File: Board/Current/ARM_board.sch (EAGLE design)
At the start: 157 parts, among them IC3 STM32F437VI, IC4 LM358DT, J1 USART/I2C, J10 ANALOG, J11 DGND, J12 DPWR, J13 DIGITAL, J14 SGND, J15 SPWR, J16 SERVO, J2 I2C2/USART3, J3 USART2, J5 SPI, J6 Bluesmirf, J7 SWD, J8 AGND, J9 APWR, Q1 STL4P2UH7, Q2 2STR1230, SW1 SW, U1 LSM330DLC, U10 BAV99, U11 BAV99, U12 USBLC6-2, U13 USBLC6-2, U14 STMPS2171MTR, U15 MC74HC164, U16 STL85N6F3, U17 ZENER-BZX384C20-E3-08, U18 ZENER-BZX384C20-E3-08, U2 RT7259, U3 NC7SZU04, U4 L6206Q, U5 L6206Q, U6 SI7617, U7 SI7617, U8 SI7617, U9 SI7617, Y2 8MHz

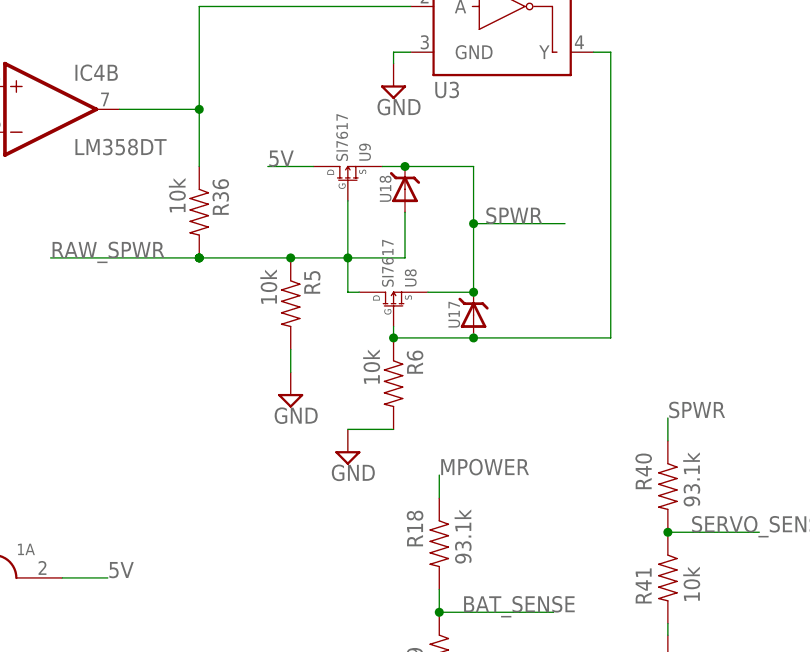
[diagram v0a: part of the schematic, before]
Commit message: Added green box 30mil inside the board outline and moved all traces within the line. Removed the extra space that was added around the board for the previous revision. Removed the zener diodes for now (need to re-evaluate them).
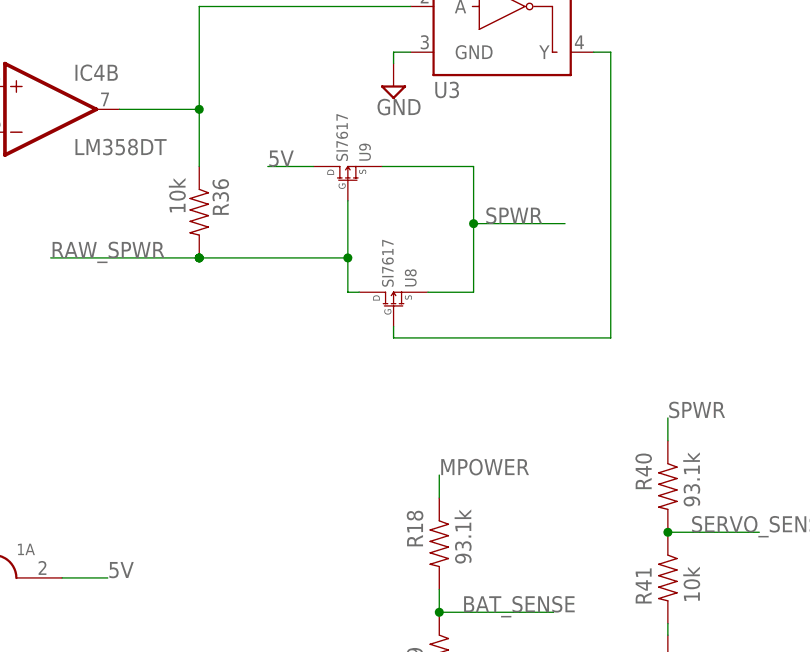
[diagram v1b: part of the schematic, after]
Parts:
- removed R5, R6: 10k, SparkFun:RESISTOR0402-RES
- removed U17, U18: ZENER-BZX384C20-E3-08, zener-BZX384C20-E3-08:ZENER-BZX384C20-E3-08
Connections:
- net GND: no longer R5.2, R6.2
- net N$30: no longer R6.1, U17.P$2
- net RAW_SPWR: no longer R5.1, U18.P$2
- net SPWR: no longer U17.P$1, U18.P$1
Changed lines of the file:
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@@
 <?xml version="1.0" encoding="utf-8"?>
 <!DOCTYPE eagle SYSTEM "eagle.dtd">
-<eagle version="6.5.0">
+<eagle version="6.3">
 <drawing>
 <settings>
@@
 <grid distance="0.1" unitdist="inch" unit="inch" style="lines" multiple="1" display="no" altdistance="0.01" altunitdist="inch" altunit="inch"/>
 <layers>
-<layer number="1" name="Top" color="4" fill="1" visible="no" active="no"/>
-<layer number="16" name="Bottom" color="1" fill="1" visible="no" active="no"/>
-<layer number="17" name="Pads" color="2" fill="1" visible="no" active="no"/>
-<layer number="18" name="Vias" color="2" fill="1" visible="no" active="no"/>
-<layer number="19" name="Unrouted" color="6" fill="1" visible="no" active="no"/>
-<layer number="20" name="Dimension" color="15" fill="1" visible="no" active="no"/>
-<layer number="21" name="tPlace" color="7" fill="1" visible="no" active="no"/>
-<layer number="22" name="bPlace" color="7" fill="1" visible="no" active="no"/>
-<layer number="23" name="tOrigins" color="15" fill="1" visible="no" active="no"/>
-<layer number="24" name="bOrigins" color="15" fill="1" visible="no" active="no"/>
-<layer number="25" name="tNames" color="7" fill="1" visible="no" active="no"/>
-<layer number="26" name="bNames" color="7" fill="1" visible="no" active="no"/>
-<layer number="27" name="tValues" color="7" fill="1" visible="no" active="no"/>
-<layer number="28" name="bValues" color="7" fill="1" visible="no" active="no"/>
+<layer number="1" name="Top" color="4" fill="1" visible="yes" active="no"/>
+<layer number="16" name="Bottom" color="1" fill="1" visible="yes" active="no"/>
+<layer number="17" name="Pads" color="2" fill="1" visible="yes" active="no"/>
+<layer number="18" name="Vias" color="2" fill="1" visible="yes" active="no"/>
+<layer number="19" name="Unrouted" color="6" fill="1" visible="yes" active="no"/>
+<layer number="20" name="Dimension" color="15" fill="1" visible="yes" active="no"/>
+<layer number="21" name="tPlace" color="15" fill="1" visible="yes" active="no"/>
+<layer number="22" name="bPlace" color="7" fill="1" visible="yes" active="no"/>
+<layer number="23" name="tOrigins" color="15" fill="1" visible="yes" active="no"/>
+<layer number="24" name="bOrigins" color="15" fill="1" visible="yes" active="no"/>
+<layer number="25" name="tNames" color="15" fill="1" visible="yes" active="no"/>
+<layer number="26" name="bNames" color="7" fill="1" visible="yes" active="no"/>
+<layer number="27" name="tValues" color="7" fill="1" visible="yes" active="no"/>
+<layer number="28" name="bValues" color="7" fill="1" visible="yes" active="no"/>
 <layer number="29" name="tStop" color="7" fill="3" visible="no" active="no"/>
 <layer number="30" name="bStop" color="7" fill="6" visible="no" active="no"/>
-<layer number="31" name="tCream" color="7" fill="4" visible="no" active="no"/>
+<layer number="31" name="tCream" color="15" fill="1" visible="no" active="no"/>
 <layer number="32" name="bCream" color="7" fill="5" visible="no" active="no"/>
 <layer number="33" name="tFinish" color="6" fill="3" visible="no" active="no"/>
@@
 <layer number="35" name="tGlue" color="7" fill="4" visible="no" active="no"/>
 <layer number="36" name="bGlue" color="7" fill="5" visible="no" active="no"/>
-<layer number="37" name="tTest" color="7" fill="1" visible="no" active="no"/>
-<layer number="38" name="bTest" color="7" fill="1" visible="no" active="no"/>
+<layer number="37" name="tTest" color="7" fill="1" visible="yes" active="no"/>
+<layer number="38" name="bTest" color="7" fill="1" visible="yes" active="no"/>
 <layer number="39" name="tKeepout" color="4" fill="11" visible="no" active="no"/>
 <layer number="40" name="bKeepout" color="1" fill="11" visible="no" active="no"/>
@@
 <layer number="44" name="Drills" color="7" fill="1" visible="no" active="no"/>
 <layer number="45" name="Holes" color="7" fill="1" visible="no" active="no"/>
-<layer number="46" name="Milling" color="3" fill="1" visible="no" active="no"/>
-<layer number="47" name="Measures" color="7" fill="1" visible="no" active="no"/>
-<layer number="48" name="Document" color="7" fill="1" visible="no" active="no"/>
-<layer number="49" name="Reference" color="7" fill="1" visible="no" active="no"/>
-<layer number="50" name="dxf" color="7" fill="1" visible="no" active="no"/>
-<layer number="51" name="tDocu" color="7" fill="1" visible="no" active="no"/>
-<layer number="52" name="bDocu" color="7" fill="1" visible="no" active="no"/>
-<layer number="53" name="tGND_GNDA" color="7" fill="9" visible="no" active="no"/>
-<layer number="54" name="bGND_GNDA" color="1" fill="9" visible="no" active="no"/>
-<layer number="56" name="wert" color="7" fill="1" visible="no" active="no"/>
+<layer number="46" name="Milling" color="3" fill="1" visible="yes" active="no"/>
+<layer number="47" name="Measures" color="7" fill="1" visible="yes" active="no"/>
+<layer number="48" name="Document" color="12" fill="1" visible="yes" active="no"/>
+<layer number="49" name="Reference" color="7" fill="1" visible="yes" active="no"/>
+<layer number="50" name="dxf" color="7" fill="1" visible="yes" active="no"/>
+<layer number="51" name="tDocu" color="7" fill="1" visible="yes" active="no"/>
+<layer number="52" name="bDocu" color="7" fill="1" visible="yes" active="no"/>
+<layer number="53" name="tGND_GNDA" color="7" fill="9" visible="yes" active="no"/>
+<layer number="54" name="bGND_GNDA" color="1" fill="9" visible="yes" active="no"/>
+<layer number="56" name="wert" color="7" fill="1" visible="yes" active="no"/>
 <layer number="91" name="Nets" color="2" fill="1" visible="yes" active="yes"/>
 <layer number="92" name="Busses" color="1" fill="1" visible="yes" active="yes"/>
@@
 <part name="R37" library="SparkFun-Resistors" deviceset="RESISTOR" device="0603-RES" value="3k"/>
 <part name="R38" library="SparkFun-Resistors" deviceset="RESISTOR" device="0603-RES" value="3k"/>
-<part name="U17" library="zener-BZX384C20-E3-08" deviceset="ZENER-BZX384C20-E3-08" device=""/>
-<part name="U18" library="zener-BZX384C20-E3-08" deviceset="ZENER-BZX384C20-E3-08" device=""/>
-<part name="R5" library="SparkFun" deviceset="RESISTOR" device="0402-RES" value="10k"/>
-<part name="R6" library="SparkFun" deviceset="RESISTOR" device="0402-RES" value="10k"/>
-<part name="SUPPLY49" library="supply2" deviceset="GND" device=""/>
-<part name="SUPPLY58" library="supply2" deviceset="GND" device=""/>
 </parts>
 <sheets>
@@
 <instance part="R37" gate="G$1" x="-224.79" y="-119.38" rot="R90"/>
 <instance part="R38" gate="G$1" x="-224.79" y="-54.61" rot="R90"/>
-<instance part="U17" gate="G$1" x="-124.46" y="36.83" smashed="yes" rot="R90">
-<attribute name="NAME" x="-125.984" y="35.306" size="1.27" layer="95" rot="R90"/>
-</instance>
-<instance part="U18" gate="G$1" x="-132.08" y="50.8" smashed="yes" rot="R90">
-<attribute name="NAME" x="-133.604" y="49.276" size="1.27" layer="95" rot="R90"/>
-</instance>
-<instance part="R5" gate="G$1" x="-144.78" y="38.1" rot="R270"/>
-<instance part="R6" gate="G$1" x="-133.35" y="29.21" rot="R270"/>
-<instance part="SUPPLY49" gate="GND" x="-138.43" y="21.59"/>
-<instance part="SUPPLY58" gate="GND" x="-144.78" y="27.94"/>
 </instances>
 <busses>
@@
 <label x="167.64" y="46.99" size="1.778" layer="95"/>
 </segment>
-<segment>
-<pinref part="R6" gate="G$1" pin="2"/>
-<pinref part="SUPPLY49" gate="GND" pin="GND"/>
-<wire x1="-138.43" y1="24.13" x2="-133.35" y2="24.13" width="0.1524" layer="91"/>
-</segment>
-<segment>
-<pinref part="R5" gate="G$1" pin="2"/>
-<pinref part="SUPPLY58" gate="GND" pin="GND"/>
-<wire x1="-144.78" y1="30.48" x2="-144.78" y2="33.02" width="0.1524" layer="91"/>
-</segment>
 </net>
 <net name="5V" class="0">
@@
 <segment>
 <wire x1="-138.43" y1="49.53" x2="-138.43" y2="43.18" width="0.1524" layer="91"/>
-<wire x1="-138.43" y1="43.18" x2="-138.684" y2="43.18" width="0.1524" layer="91"/>
 <pinref part="R36" gate="G$1" pin="2"/>
 <label x="-171.45" y="43.18" size="1.778" layer="95"/>
-<wire x1="-138.684" y1="43.18" x2="-144.78" y2="43.18" width="0.1524" layer="91"/>
-<wire x1="-144.78" y1="43.18" x2="-154.94" y2="43.18" width="0.1524" layer="91"/>
+<wire x1="-138.43" y1="43.18" x2="-154.94" y2="43.18" width="0.1524" layer="91"/>
 <wire x1="-154.94" y1="43.18" x2="-171.45" y2="43.18" width="0.1524" layer="91"/>
 <junction x="-154.94" y="43.18"/>
@@
 <wire x1="-138.43" y1="39.37" x2="-138.43" y2="43.18" width="0.1524" layer="91"/>
 <junction x="-138.43" y="43.18"/>
-<pinref part="U18" gate="G$1" pin="P$2"/>
-<wire x1="-132.08" y1="48.26" x2="-132.08" y2="43.18" width="0.1524" layer="91"/>
-<wire x1="-132.08" y1="43.18" x2="-138.43" y2="43.18" width="0.1524" layer="91"/>
-<pinref part="R5" gate="G$1" pin="1"/>
-<junction x="-144.78" y="43.18"/>
 </segment>
 </net>
@@
 <pinref part="U8" gate="G$1" pin="G"/>
 <wire x1="-133.35" y1="35.56" x2="-133.35" y2="34.29" width="0.1524" layer="91"/>
-<wire x1="-133.35" y1="34.29" x2="-124.46" y2="34.29" width="0.1524" layer="91"/>
-<pinref part="U17" gate="G$1" pin="P$2"/>
-<wire x1="-124.46" y1="34.29" x2="-109.22" y2="34.29" width="0.1524" layer="91"/>
-<junction x="-124.46" y="34.29"/>
-<pinref part="R6" gate="G$1" pin="1"/>
-<junction x="-133.35" y="34.29"/>
+<wire x1="-133.35" y1="34.29" x2="-109.22" y2="34.29" width="0.1524" layer="91"/>
 </segment>
 </net>
@@
 <pinref part="U8" gate="G$1" pin="S"/>
 <pinref part="U9" gate="G$1" pin="S"/>
-<wire x1="-124.46" y1="53.34" x2="-132.08" y2="53.34" width="0.1524" layer="91"/>
-<wire x1="-132.08" y1="53.34" x2="-134.62" y2="53.34" width="0.1524" layer="91"/>
+<wire x1="-124.46" y1="53.34" x2="-134.62" y2="53.34" width="0.1524" layer="91"/>
 <wire x1="-124.46" y1="46.99" x2="-114.3" y2="46.99" width="0.1524" layer="91"/>
 <junction x="-124.46" y="46.99"/>
-<pinref part="U17" gate="G$1" pin="P$1"/>
-<junction x="-124.46" y="39.37"/>
-<pinref part="U18" gate="G$1" pin="P$1"/>
-<junction x="-132.08" y="53.34"/>
-</segment>
-<segment>
+</segment>
+<segment>

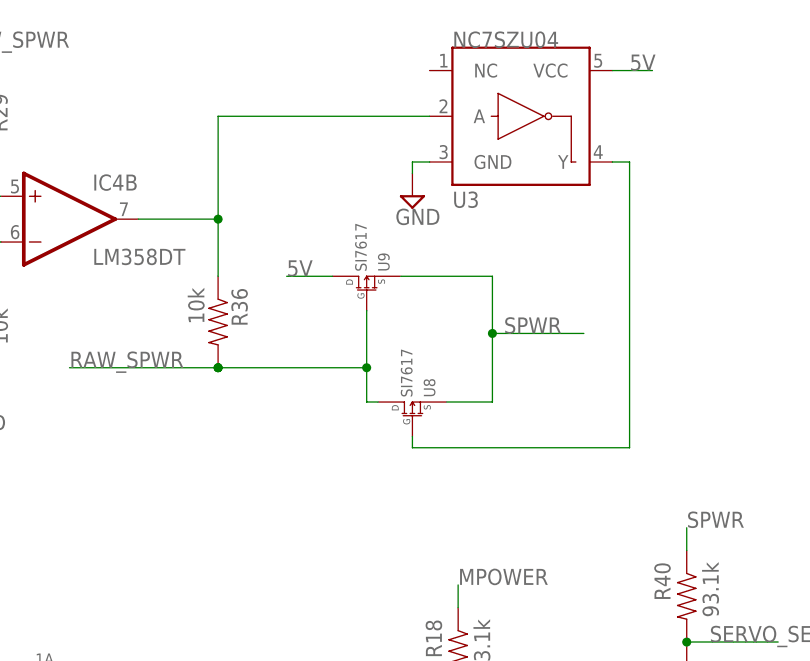
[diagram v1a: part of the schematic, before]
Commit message: Changed servo power select resistors.
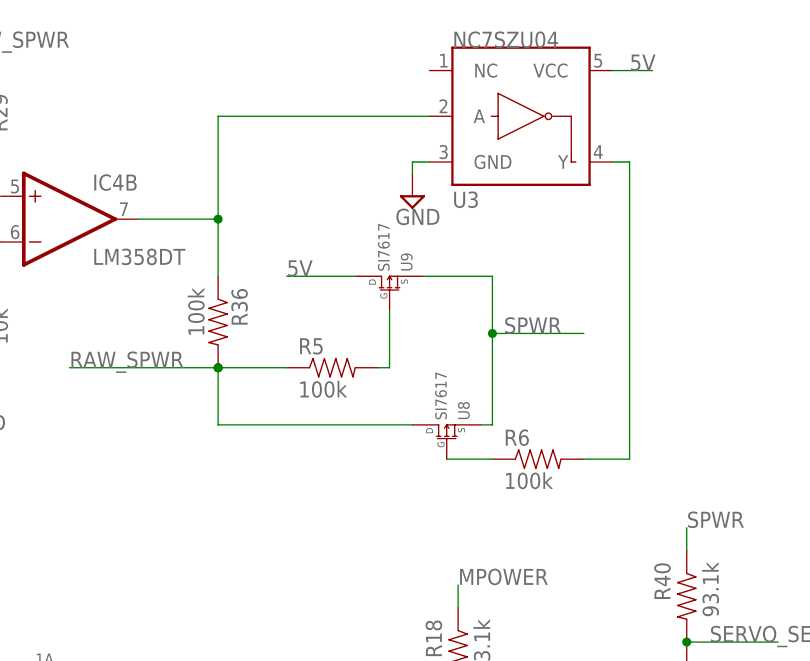
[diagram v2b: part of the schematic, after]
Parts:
- added R5, R6: 100k, SparkFun:RESISTOR0402-RES
- R36: value 10k -> 100k
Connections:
- new net N$50: R5.2, U9.G
- new net N$53: R6.1, U8.G
- net N$30: now also R6.2; no longer U8.G
- net RAW_SPWR: now also R5.1; no longer U9.G
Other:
- moved on the sheet: U8, U9

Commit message: Starting updating the schematic for the new switching regulator.
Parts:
- removed AP1084: AP1084, r_cubed:AP1084
- removed C1, C33: 10u, SparkFun:CAP0603-CAP
- removed C26, C28: 10u, SparkFun:CAP0805
- removed C3, C36, C4, C5: 22u, SparkFun:CAP0805
- removed C31: 22u, SparkFun:CAP1206
- removed C32: 1u, SparkFun:CAP0603-CAP
- removed C38: 0.1u, SparkFun:CAP0402-CAP
- removed C8: 100u, SparkFun:CAP_POLD
- removed L1: 2.7u, r_cubed:INDUCTOR
- removed R32: 93.1k, SparkFun:RESISTOR0402-RES
- removed R33: 18k, SparkFun:RESISTOR0402-RES
- removed R34: 100k, SparkFun:RESISTOR0402-RES
- removed R44: 2k, SparkFun:RESISTOR0402-RES
- removed R45: 1.21k, SparkFun:RESISTOR0402-RES
- removed U16: STL85N6F3, r_cubed:STL85N6F3
- removed U2: RT7259, r_cubed:SWITCHING_REG
- added C51, C53, C54, C55, C57, C58, C59, C60, C61: ?, SparkFun:CAP0402-CAP
- added C52: ?, SparkFun:CAP_POLD
- added D1, D2, D3, D4: (no value), SparkFun:DIODESMA
- added L2, L3: ?, r_cubed:INDUCTOR
- added R14, R15, R16, R8, R9: ?, SparkFun:RESISTOR0402-RES
- added R17, R30, R50: 100k, SparkFun:RESISTOR0402-RES
- added U$1: PM6685, r_cubed:PM6685
- added U17, U18, U19, U20: ?, r_cubed:STL85N6F3
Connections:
- removed net MPOWER: C11.1, C20.1, C26.1, C28.1, C31.1, C48.1, C8.+, C9.1, JP3.8, R10.2, R18.1, R34.2, U10.1, U11.1, U2.VIN, U4.VS, U5.VS, U7.D
- removed net N$10: C32.2, L1.1, U16.D, U2.SW
- removed net N$17: R32.1, R33.2, U2.FB
- removed net N$20: C33.2, U2.VCC
- removed net N$25: C32.1, U2.BOOT
- removed net N$32: AP1084.ADJ, C38.2, R44.2, R45.1
- removed net N$35: U16.G, U2.BG
- removed net N$44: R34.1, U2.EN/SYNC
- new net N$55: R8.2, U$1.CSENSE5
- new net N$56: U$1.HGATE5, U17.G
- new net N$57: U$1.LGATE5, U18.G
- new net N$59: C51.1, D3.C, U$1.BOOT5
- new net N$66: C51.2, D1.C, L2.1, R8.1, U$1.PHASE5, U17.S, U18.D
- new net N$67: C54.2, R9.1
- new net N$69: C53.1, C54.1, U$1.COMP5
- new net N$72: U$1.LGATE3, U20.G
- new net N$73: U$1.HGATE3, U19.G
- new net N$74: C55.1, D4.C, U$1.BOOT3
- new net N$75: C55.2, D2.C, L3.1, R14.1, U$1.PHASE3, U19.S, U20.D
- new net N$76: R14.2, U$1.CSENSE3
- new net N$77: C57.1, C58.1, U$1.COMP3
- new net N$78: C58.2, R15.1
- new net N$79: C59.1, R16.2, U$1.VIN
- new net N$80: C60.1, U$1.VREF
- new net N$81: C61.1, U$1.FSEL, U$1.LDO5, U$1.VCC
- new net N$82: R30.2, U$1.SHUDN
- new net N$83: R17.2, U$1.EN3
- new net N$84: R50.2, U$1.EN5
- new net VIN: C11.1, C20.1, C48.1, C9.1, D3.A, D4.A, JP3.8, R10.2, R16.1, R17.1, R18.1, R30.1, R50.1, U10.1, U11.1, U17.D, U19.D, U4.VS, U5.VS, U7.D
- net +3V3: now also L3.2, R15.2, U$1.OUT3; no longer AP1084.VOUT, C38.1, R45.2
- net 5V: now also C52.+, L2.2, R9.2, U$1.OUT5; no longer AP1084.VIN, C1.1, C3.1, C36.1, C4.1, C5.1, L1.2, R32.2
- net GND: now also C52.-, C53.2, C57.2, C59.2, C60.2, C61.2, D1.A, D2.A, U$1.LDO3SEL, U$1.PGND, U$1.SGND, U$1.SGND2, U$1.SKIP, U$1.V5SW, U18.S, U20.S; no longer C1.2, C26.2, C28.2, C3.2, C31.2, C33.1, C36.2, C4.2, C5.2, C8.-, R33.1, R44.1, U16.S, U2.GND
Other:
- moved on the sheet: C25, C29, C34, C35, C39, C40, C41, C42, C43, C44, C46, C47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

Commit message: Made more progress on switching regulator.
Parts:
- removed C51: ?, SparkFun:CAP0402-CAP
- removed L3: ?, r_cubed:INDUCTOR
- added C1, C8: 0.1u, SparkFun:CAP0402-CAP
- added C3, C4: 15u, SparkFun:CAP0402-CAP
- added C5: 1u, SparkFun:CAP0402-CAP
- added L1: 1.5uH, r_cubed:INDUCTOR
- added R32: 47, SparkFun:RESISTOR0402-RES
- C53, C57: value ? -> 47p
- C55, C60: value ? -> 0.1u
- C58: value ? -> 100p
- C59, C61: value ? -> 4.7u
- D1, D2: value (none) -> STPS1L30M; device SparkFun:DIODESMA -> SparkFun:DIODE-SCHOTTKY_
- L2: value ? -> 3.3uH
- R15: value ? -> 1k
- R16: value ? -> 3.9
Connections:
- removed net N$59: C51.1, D3.C, U$1.BOOT5
- removed net N$81: C61.1, U$1.FSEL, U$1.LDO5, U$1.VCC
- new net LDO5: C61.1, R32.2, U$1.FSEL, U$1.LDO5
- new net N$20: C5.1, R32.1, U$1.VCC
- new net N$25: C8.1, D3.C, U$1.BOOT5
- net +3V3: now also L2.2; no longer L3.2
- net 5V: now also L1.2; no longer L2.2
- net GND: now also C1.2, C3.2, C4.2, C5.2
- net N$66: now also C8.2, L1.1; no longer C51.2, L2.1
- net N$75: now also L2.1; no longer L3.1
- net N$79: now also C1.1
- net VIN: now also C3.1, C4.1
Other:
- moved on the sheet: BTN0, BTN1, C10, C11, C12, C13, C14, C15, C16, C17, C18, C19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
